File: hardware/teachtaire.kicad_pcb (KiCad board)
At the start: 6 copper layers, 60 x 60 mm, 83 parts, among them J1 39-29-1048, J2 ESQ-110-X-X-D, J3 Conn_Coaxial, J4 5023860570, J5 Conn_Coaxial, Q1 NMOS, Q2 IPD90P04P4L04ATMA1, Q3 PMOS, Q4 NMOS, U1 MAX-M10S, U2 STM32F072C8Tx, U3 TJA1051T/3/1J, U4 RF-LORA-868-SO, U5 LT6003HDC-TRMPBF, U6 NC7WZ07P6X, U7 NC7WZ07P6X, U8 MPM3650CGQW-P, U9 TLV75533PDRV

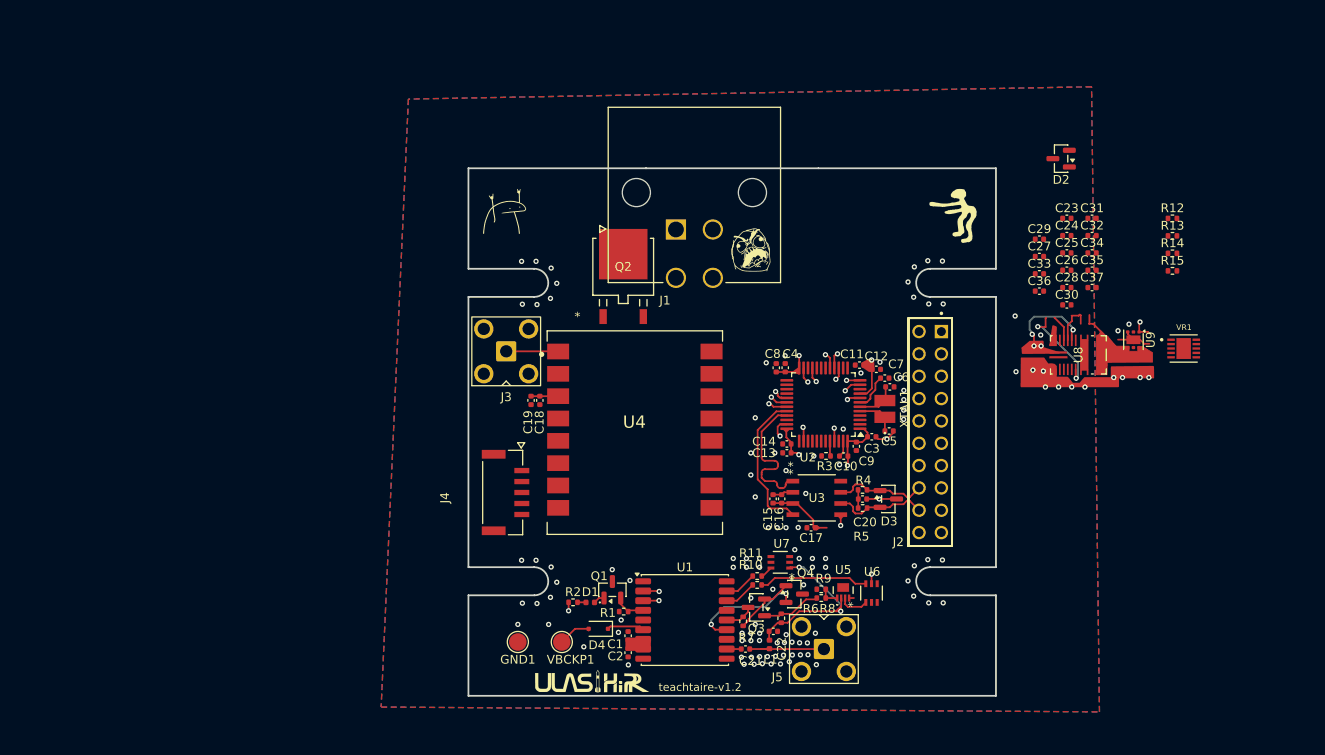
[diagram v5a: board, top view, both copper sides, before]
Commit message: power and main routing done, just need to set rf trace width
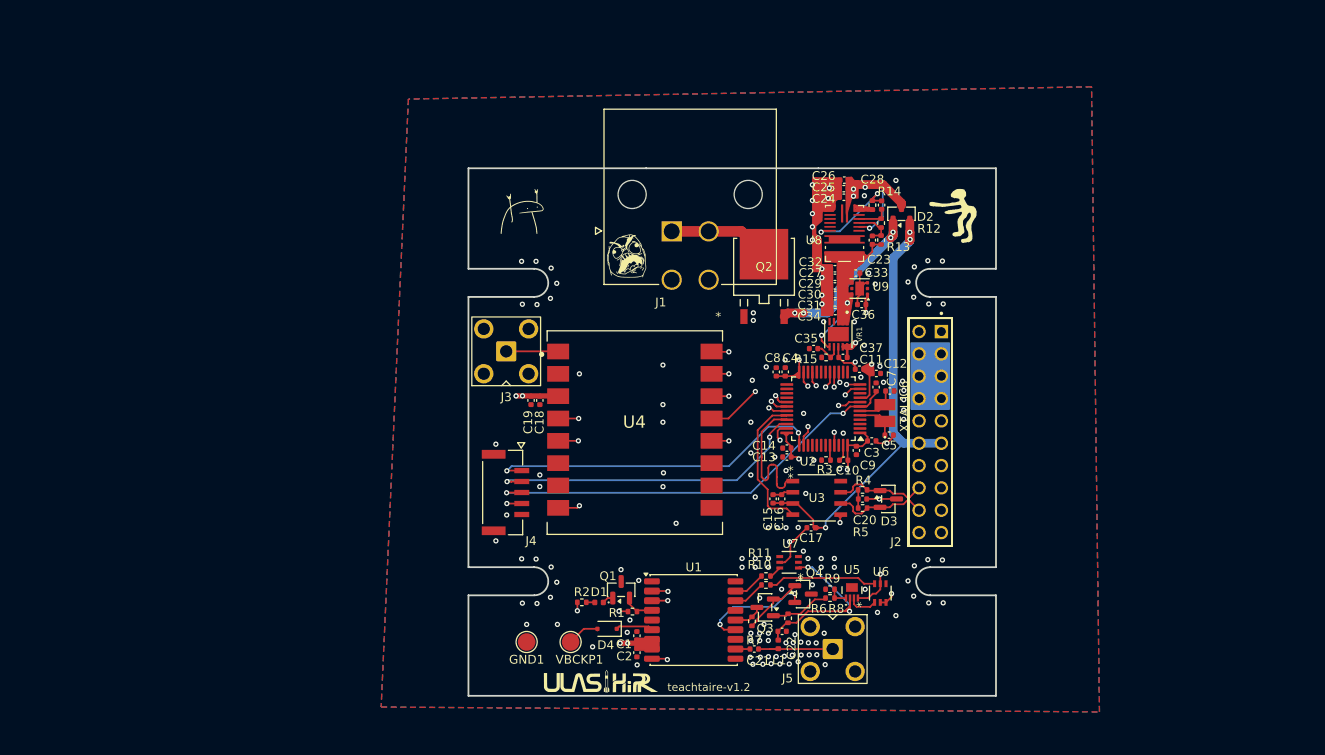
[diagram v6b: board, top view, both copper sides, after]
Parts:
- moved R15 40.6 mm to (161.6, 86.6), turned to 180 degrees
- moved VR1 39.3 mm to (163.0, 84.0), turned to -90 degrees
- moved R14 34.6 mm to (166.8, 69.3), turned to 90 degrees
- moved R13 33.1 mm to (167.8, 73.3), turned to -90 degrees
- moved R12 33.1 mm to (167.8, 71.4), turned to -90 degrees
- moved C35 32.9 mm to (160.1, 85.6)
- moved U9 31.7 mm to (165.4, 78.8), turned to 180 degrees
- moved C31 30.8 mm to (162.6, 80.4), turned to 180 degrees
- moved U8 30.0 mm to (163.7, 72.5), turned to 0 degrees
- moved C34 30.0 mm to (162.6, 81.4)
- moved C32 29.5 mm to (162.6, 76.5), turned to 180 degrees
- moved C37 29.4 mm to (163.5, 86.6), turned to 180 degrees
- moved C26 27.3 mm to (163.6, 66.5)
- moved C25 26.4 mm to (163.6, 67.4)
- moved C30 26.4 mm to (162.6, 79.5), turned to 180 degrees
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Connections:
- D2 pad 1: 5VLOGIC -> Net-(Q2-S)
- D2 pad 2: Net-(Q2-S) -> 5VLOGIC
- J4 pad 4: +3.3V -> +3V3D
- R2 pad 1: +3.3V -> +3V3D
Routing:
- net +3V3D: track 25.8 -> 140.6 mm, vias 7 -> 11
- net +3V3RF: track 3.08 -> 95.2 mm, vias 0 -> 5
- net 5VLOGIC: track 7.56 -> 53.5 mm, vias 0 -> 3
- net NRST: track 4.18 -> 48.9 mm, vias 0 -> 2
- net SWCLK: track 0.00 -> 38.8 mm, vias 0 -> 2
- net LoRa_DIO2: track 1.72 -> 39.6 mm, vias 1 -> 2
- net SWDIO: track 0.00 -> 37.1 mm, vias 0 -> 2
- net GNSS_RESET: track 1.49 -> 38.1 mm, vias 1 -> 2
- net GND: track 24.7 -> 57.8 mm, vias 124 -> 149
- net LoRa_TX_SWITCH: track 1.60 -> 31.4 mm, vias 1 -> 2
- net PA9: track 3.81 -> 32.1 mm
- net LoRa_RX_SWITCH: track 1.71 -> 27.5 mm, vias 1 -> 2
- net PA10: track 4.02 -> 29.7 mm
- net Net-(Q2-S): track 0.00 -> 20.3 mm, vias 0 -> 4
- net LoRa_RESET: track 1.96 -> 20.9 mm, vias 1 -> 2
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
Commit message: good to go
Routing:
- net GND: vias 149 -> 174

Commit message: ddio pins
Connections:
- U2 pad 21: LoRa_DIO2 -> LoRa_DIO0
- U2 pad 22: unconnected-(U2-PB11-Pad22) -> LoRa_DIO1
- U2 pad 25: unconnected-(U2-PB12-Pad25) -> LoRa_DIO2
- U2 pad 26: unconnected-(U2-PB13-Pad26) -> LoRa_DIO3
- U2 pad 27: unconnected-(U2-PB14-Pad27) -> LoRa_DIO4
- U2 pad 28: unconnected-(U2-PB15-Pad28) -> LoRa_DIO5
- U4 pad 10: unconnected-(U4-DIO4-Pad10) -> LoRa_DIO4
- U4 pad 11: unconnected-(U4-DIO5-Pad11) -> LoRa_DIO5
- U4 pad 6: unconnected-(U4-DIO0-Pad6) -> LoRa_DIO0
- U4 pad 7: unconnected-(U4-DIO1-Pad7) -> LoRa_DIO1
- U4 pad 9: unconnected-(U4-DIO3-Pad9) -> LoRa_DIO3
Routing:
- net LoRa_DIO1: track 0.00 -> 44.7 mm, vias 0 -> 2
- net LoRa_DIO3: track 0.00 -> 42.0 mm, vias 0 -> 2
- net LoRa_DIO0: track 0.00 -> 37.8 mm, vias 0 -> 2
- net LoRa_DIO4: track 0.00 -> 23.6 mm, vias 0 -> 3
- net LoRa_DIO5: track 0.00 -> 18.9 mm, vias 0 -> 2
- net GND: track 57.8 -> 74.4 mm, vias 174 -> 178
- net LoRa_DIO2: track 39.6 -> 41.2 mm
- net +3V3D: track 140.6 -> 142.1 mm
- net LoRa_MISO: track 16.7 -> 17.6 mm
